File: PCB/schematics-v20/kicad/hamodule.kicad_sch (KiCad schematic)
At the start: 90 parts, among them J1 Conn_01x02_Male, J10 DoNotConnect, J11 2604-1104, J12 2604-1104, J13 EspSense, J14 Conn_01x02_Male, J2 2604-1102, J3 GND|5V, J4 GND|3.3V, J5 Jumper, J6 Conn_01x02_Male, J7 Current Jumper, J8 EspRelays, J9 USB_C_Receptacle_USB2.0, K1 PCN-105D, K2 PCN-105D, K3 PCN-105D, K4 PCN-105D, Q1 SS8050-SMD, Q2 SS8050, SW1 Switch, SW2 Switch, U1 LD1117AV33, U2 ESP32-WROOM-32E, U3 CP2102N-A01-GQFN28, U4 ULN2003A, U5 LDA210-PDIP, U6 LDA210-PDIP, U7 SHT4x

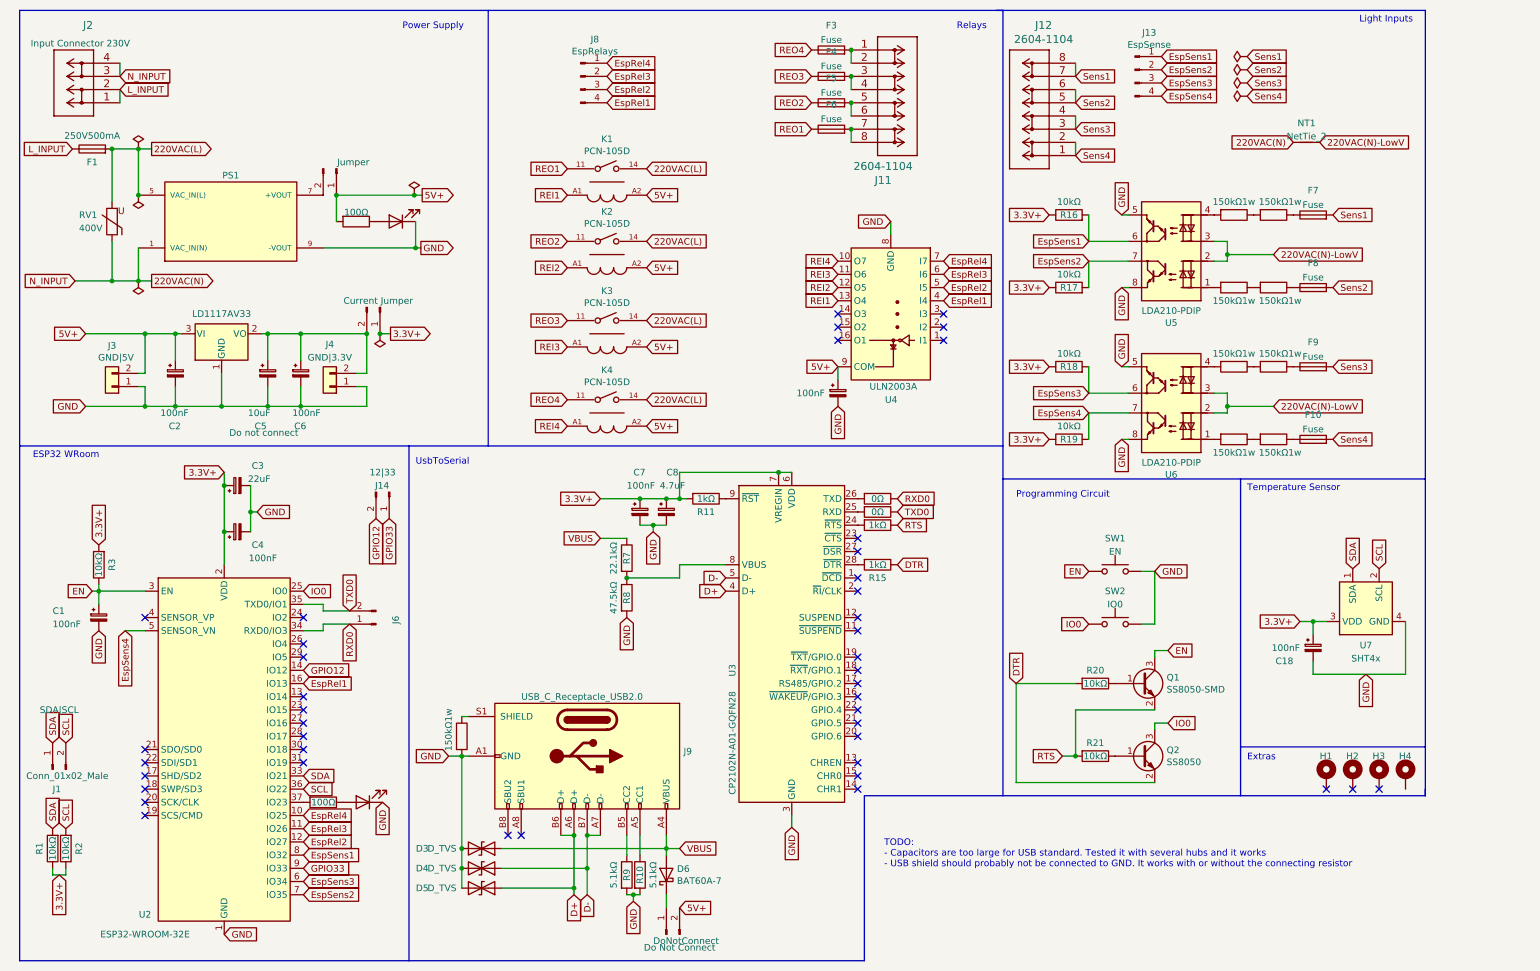
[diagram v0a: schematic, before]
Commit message: added 5v selector between USB and PS
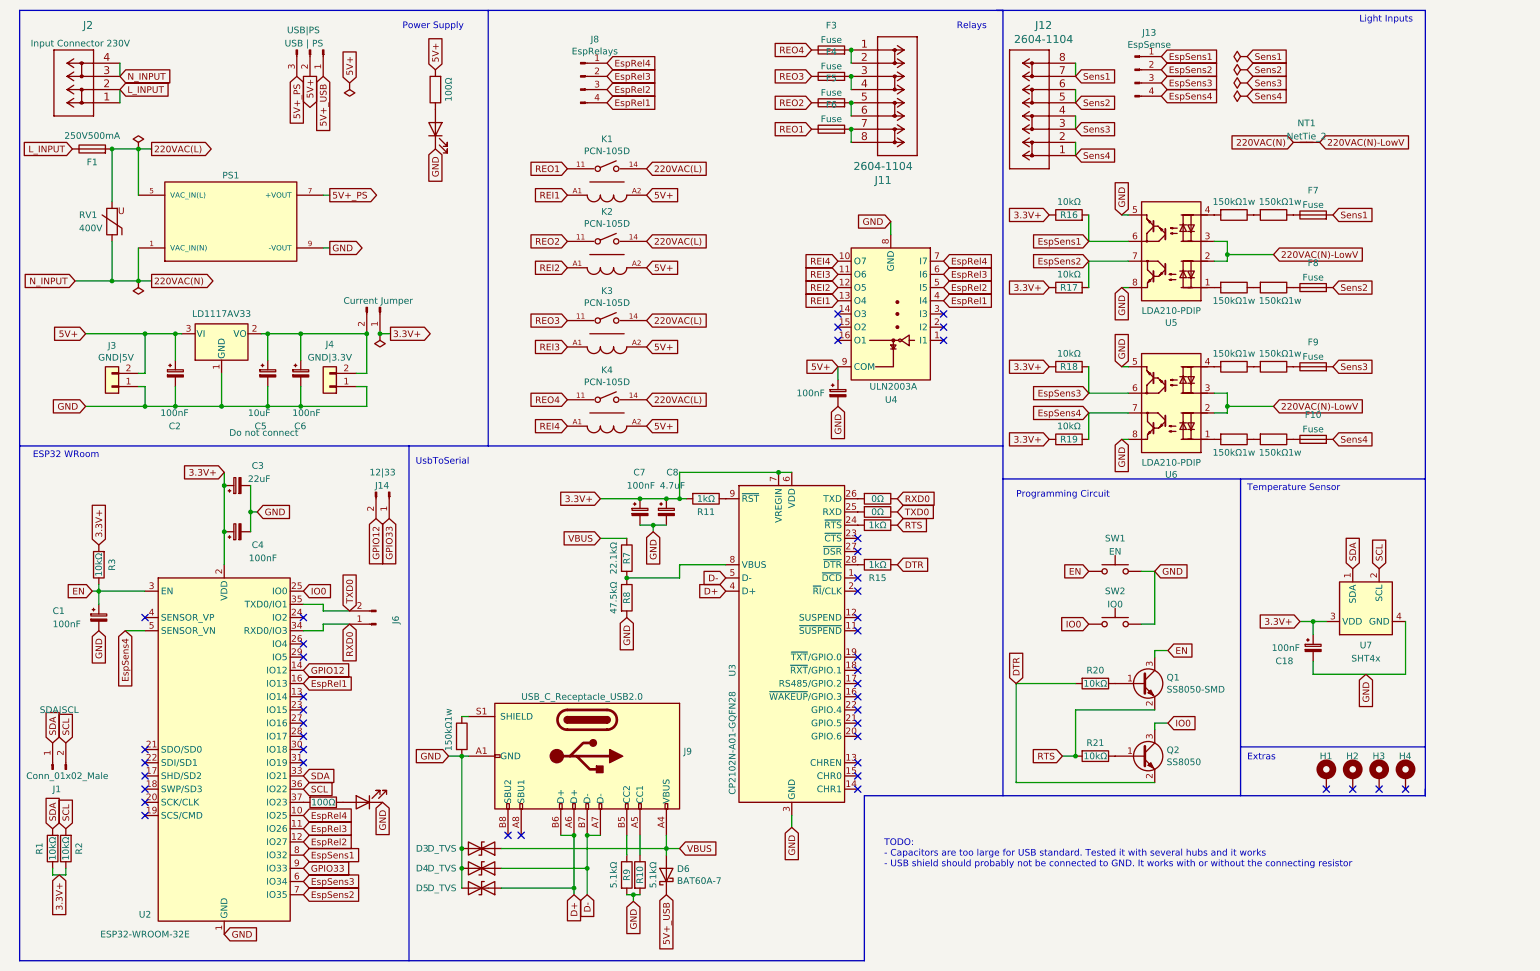
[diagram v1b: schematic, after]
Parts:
- removed J5: Jumper, Connector_PinHeader_2.54mm:PinHeader_1x02_P2.54mm_Vertical, symbol Connector:Conn_01x02_Male
- J10: value DoNotConnect -> USB | PS; footprint Connector_PinHeader_2.54mm:PinHeader_1x02_P2.54mm_Vertical -> Connector_PinHeader_2.54mm:PinHeader_1x03_P2.54mm_Vertical; symbol Connector:Conn_01x02_Male -> Connector:Conn_01x03_Male; Field4 Do Not Connect -> (none); PcbText (none) -> USB|PS
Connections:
- net 5V+_PS: now reaches PS1.7 (+VOUT)
- net 5V+_PS: now also J10.3 (Pin_3)
- net 5V+_USB: now reaches D6.1 (K), J10.1 (Pin_1)
- no-connect marks 43 -> 44

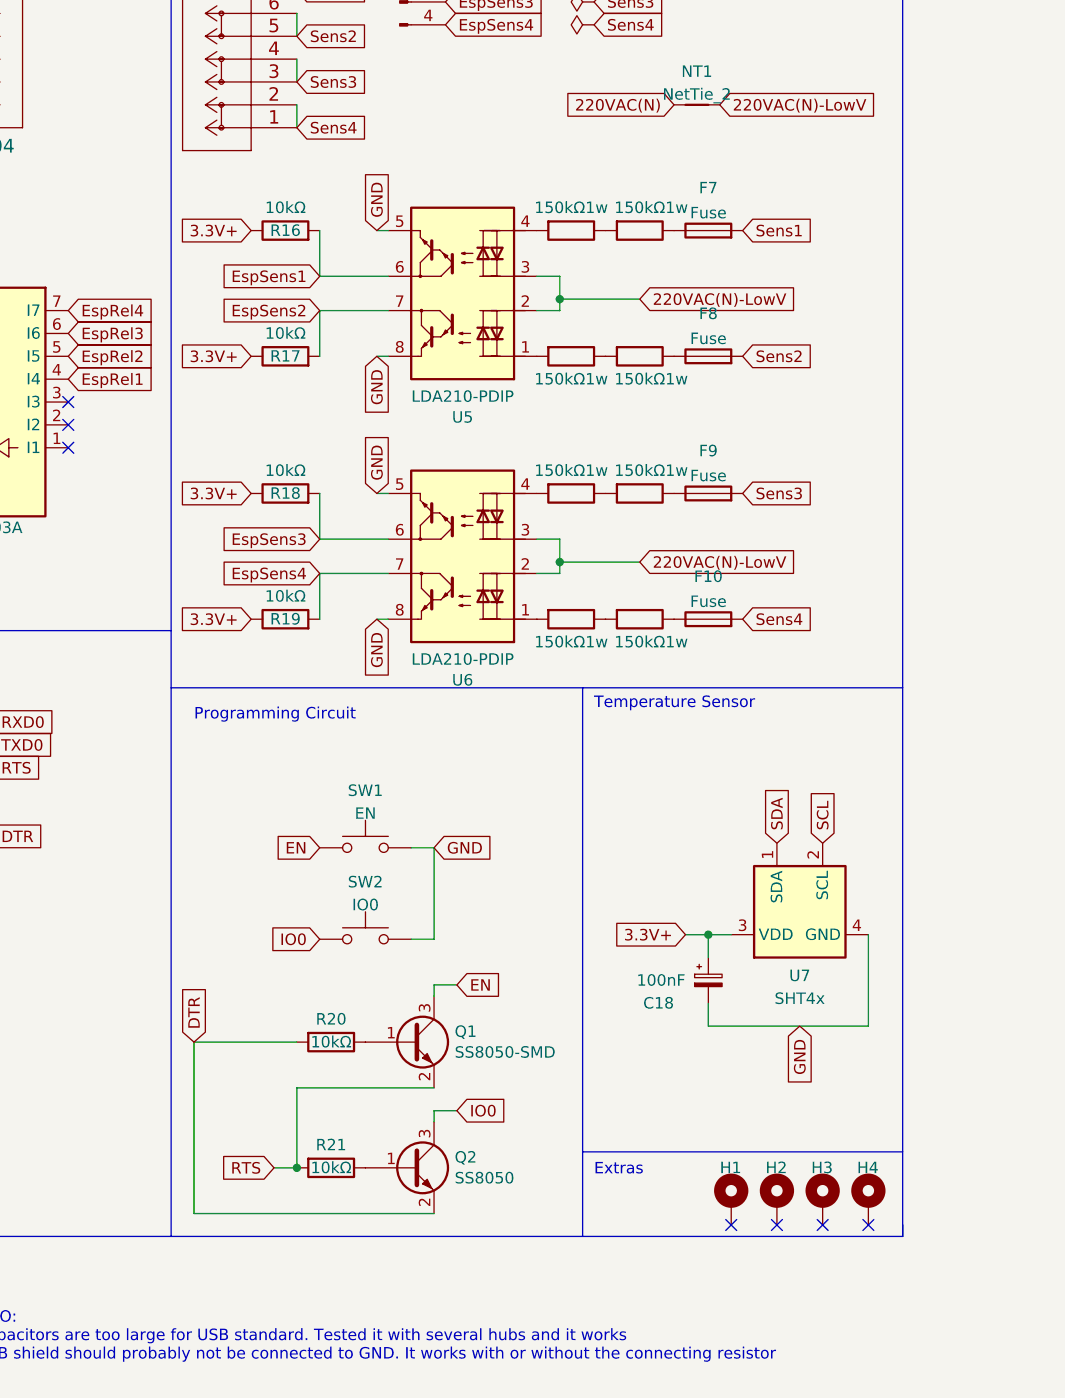
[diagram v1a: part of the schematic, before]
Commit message: reversing sensing, to make a more stable reading
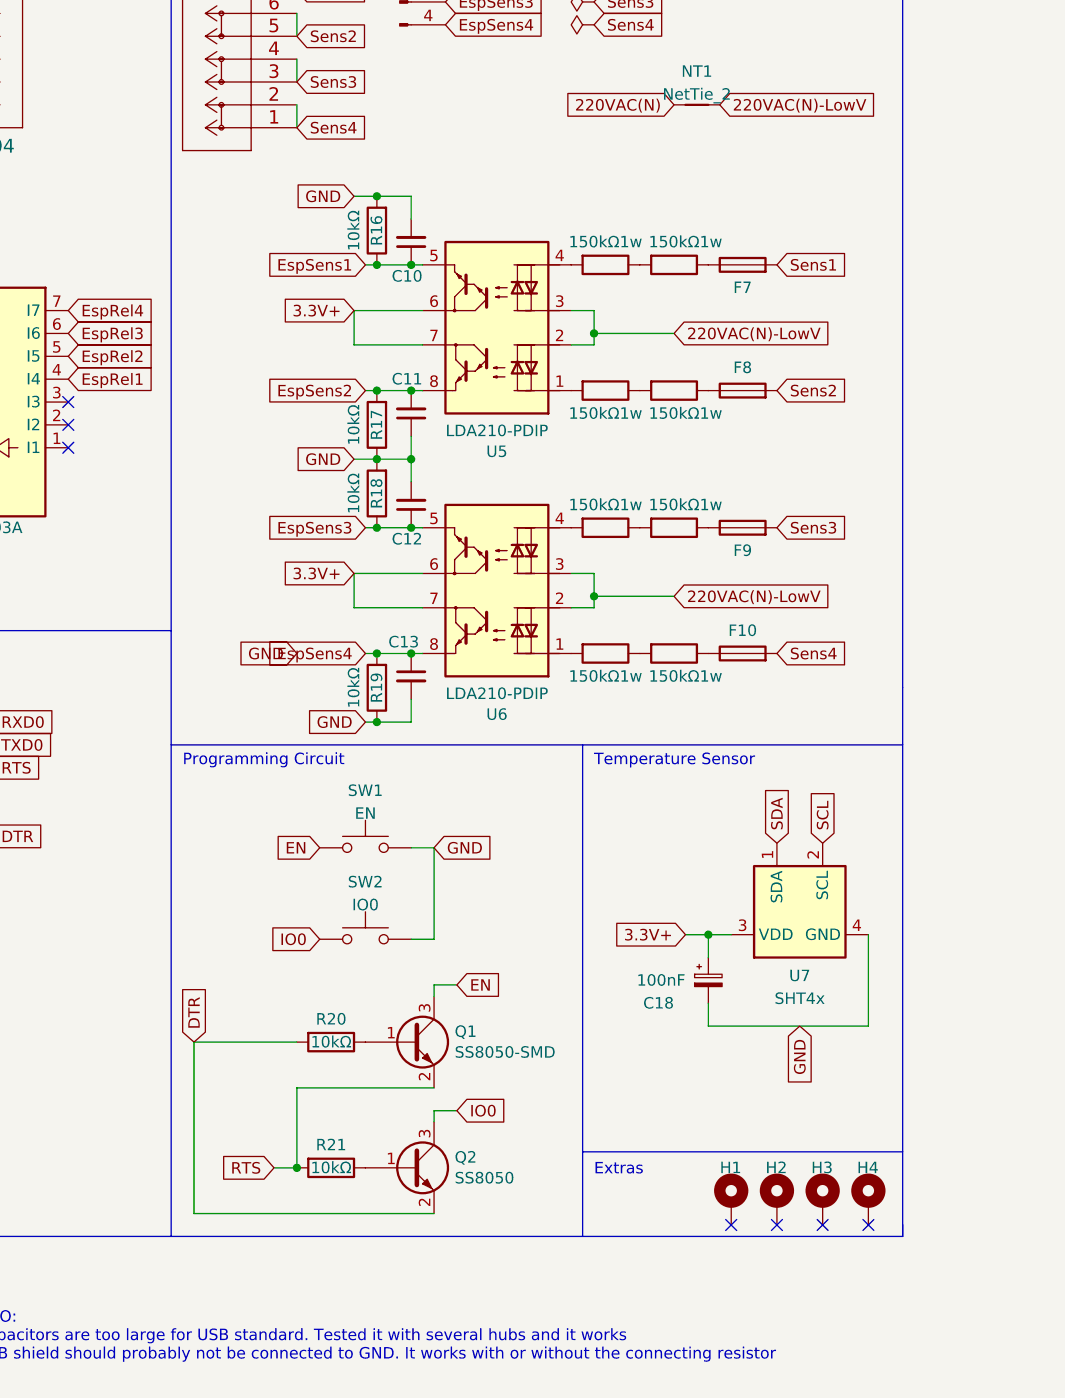
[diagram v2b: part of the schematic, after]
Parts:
- added C10, C11, C12, C13: 22uF, Capacitor_SMD:C_0603_1608Metric_Pad1.08x0.95mm_HandSolder, symbol Device:C_Small
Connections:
- net 3.3V+: now also U5.6, U5.7, U6.6, U6.7; no longer R16.1, R17.1, R18.1, R19.1
- net EspSens1: now also R16.1, U5.5, C10.1; no longer R16.2, U5.6
- net EspSens2: now also U5.8, C11.2; no longer U5.7
- net EspSens3: now also R18.1, U6.5, C12.1; no longer R18.2, U6.6
- net EspSens4: now also U6.8, C13.1; no longer U6.7
- net GND: now also R16.2, R17.1, R18.2, R19.1, C10.2, C11.1, C12.2, C13.2; no longer U5.5, U5.8, U6.5, U6.8
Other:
- moved on the sheet: F10, F7, F8, F9, R16, R17, R18, R19, U5, U6

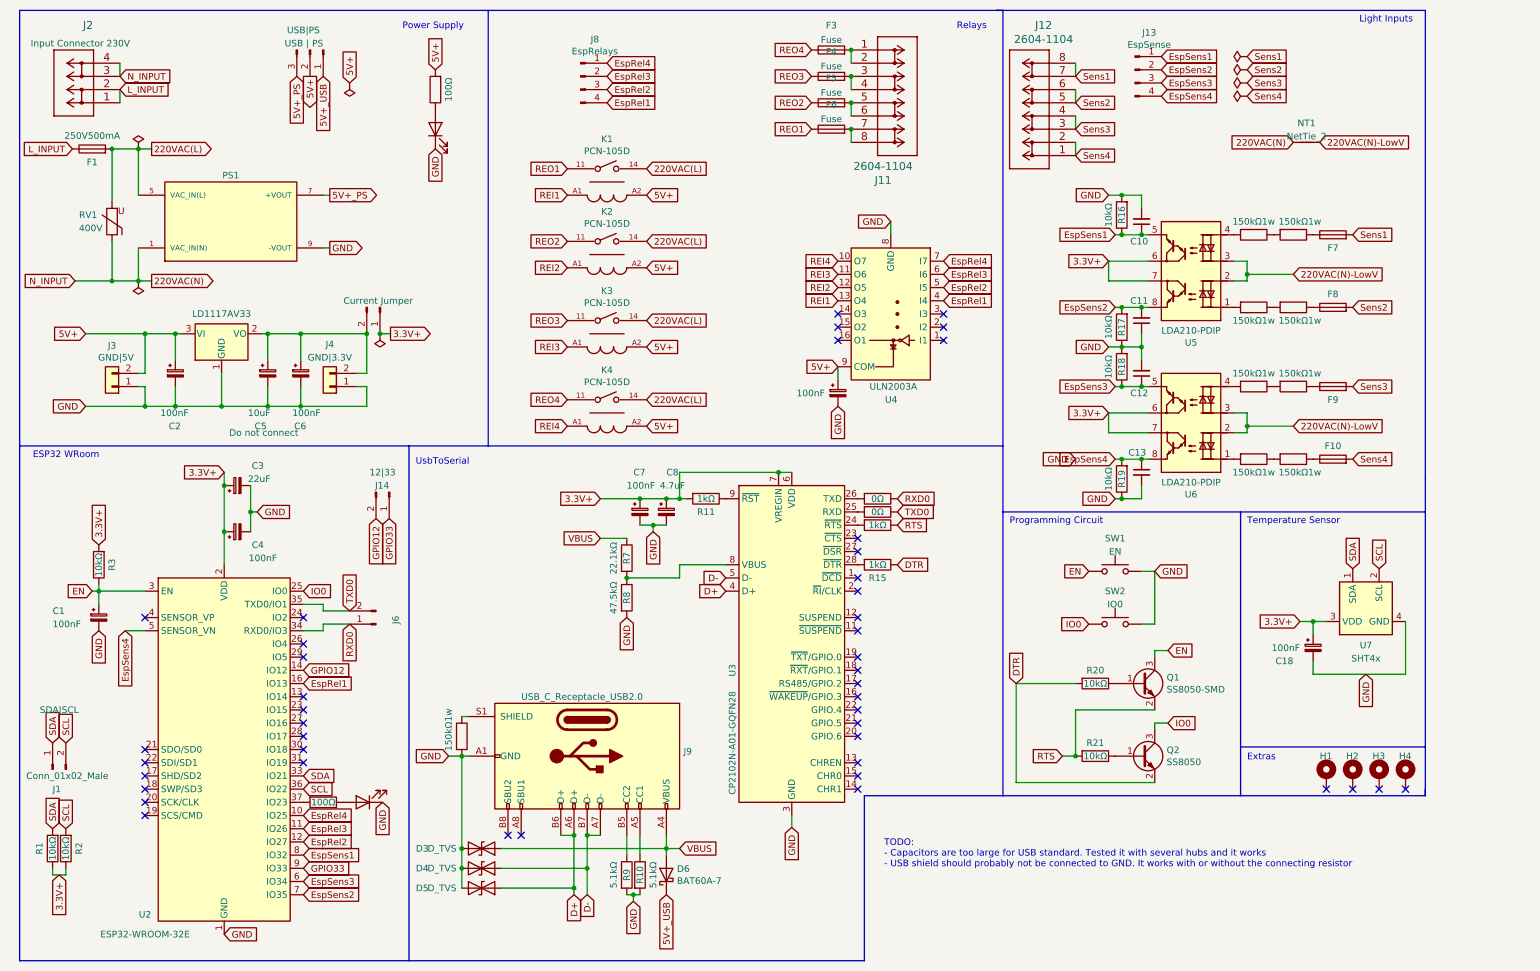
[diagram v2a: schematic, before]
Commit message: changing relays to AQG12205
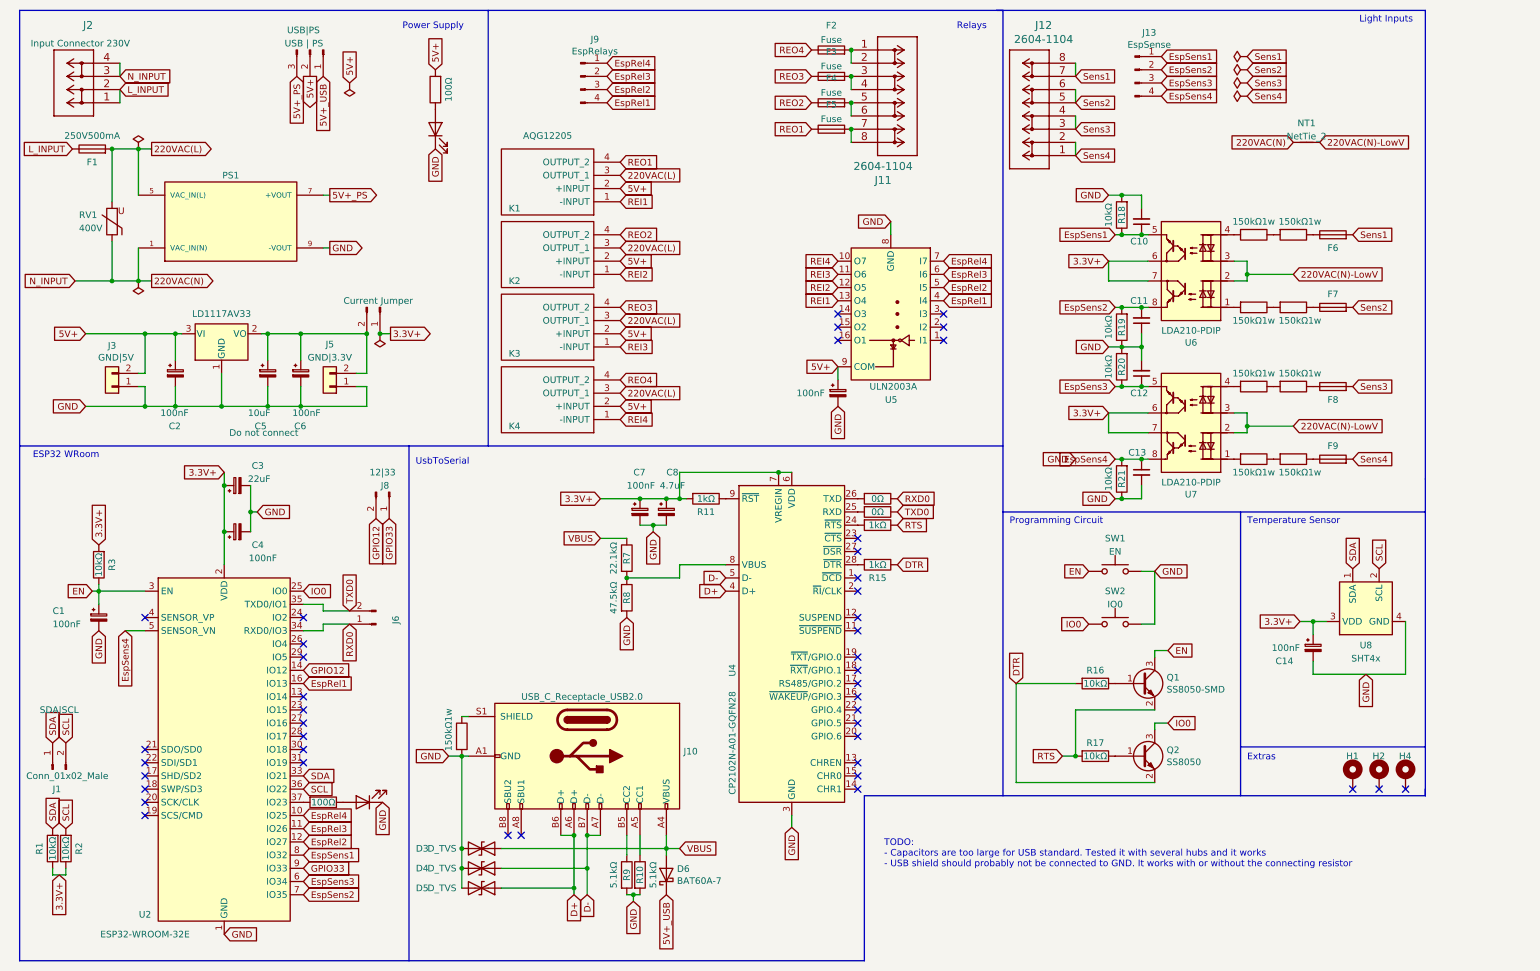
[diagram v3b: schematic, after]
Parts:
- removed H3: MountingHole_Pad, MountingHole:MountingHole_3.2mm_M3_ISO14580_Pad, symbol Mechanical:MountingHole_Pad
- removed K1, K2, K3, K4: PCN-105D, PCN:bigpads_TE_Connectivity-PCN-124D, symbol pcn-105D3:PCN-124D3MHZ,000
- added K1, K2, K3, K4: AQG12205, AQG12205, symbol AQG12205:AQG12205
- renumbered C18 to C14, F3 to F2, F4 to F3, F5 to F4, F6 to F5, F7 to F6, F8 to F7, F9 to F8, F10 to F9, J9 to J10, J10 to J4, J4 to J5, J14 to J8, J8 to J9, R20 to R16, R21 to R17, R16 to R18, R17 to R19, R18 to R20, R19 to R21, U3 to U4, U4 to U5, U5 to U6, U6 to U7, U7 to U8
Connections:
- net 220VAC(L): now also K1.3 (OUTPUT_1), K2.3 (OUTPUT_1), K3.3 (OUTPUT_1), K4.3 (OUTPUT_1)
- net 5V+: now also K1.2 (+INPUT), K2.2 (+INPUT), K3.2 (+INPUT), K4.2 (+INPUT)
- net REI1: now also K1.1 (-INPUT)
- net REI2: now also K2.1 (-INPUT)
- net REI3: now also K3.1 (-INPUT)
- net REI4: now also K4.1 (-INPUT)
- net REO1: now also K1.4 (OUTPUT_2)
- net REO2: now also K2.4 (OUTPUT_2)
- net REO3: now also K3.4 (OUTPUT_2)
- net REO4: now also K4.4 (OUTPUT_2)
- no-connect marks 44 -> 43
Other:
- moved on the sheet: H1, H2
